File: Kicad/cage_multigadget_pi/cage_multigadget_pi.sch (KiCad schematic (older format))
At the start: 41 parts, among them J1 USB_B_Micro, J2 Raspberry_Pi_2_3, Q1 BSN20, Q2 BSN20, Q3 BSN20, Q4 BSN20, Q5 BSN20, U1 OP495, U2 MCP3004, U3 LED_shift_register_SPI, U4 MultigadgetDevice, U5 MultigadgetDevice, U6 LED_Button_connector, U7 LED_Button_connector, U8 LED_Button_connector, U9 LED_Button_connector

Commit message: added reward line, changed 2x40 pin header to 2x20 header, changed USB footprint and shifted
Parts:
- added J3: Conn_01x02, Socket_Strips:Socket_Strip_Straight_1x02_Pitch2.54mm, symbol Connector_Generic:Conn_01x02
- J1: footprint Connector_USB:USB_Micro-B_Amphenol_10103594-0001LF_Horizontal -> Digikey_footprints:USB_Micro_B_Female_10118194-0001LF
- J2: footprint Connector_PinSocket_2.54mm:PinSocket_2x40_P2.54mm_Vertical -> Pin_Headers:Pin_Header_Straight_2x20_Pitch2.54mm
- U3: symbol additional_LED_drivers:LED_shift_register_SPI -> cage_multigadget_pi-rescue:LED_shift_register_SPI-additional_LED_drivers
- U4, U5: symbol MillerLab_CommonComponents:MultigadgetDevice -> cage_multigadget_pi-rescue:MultigadgetDevice-MillerLab_CommonComponents
- U6, U7, U8, U9: symbol MillerLab_CommonComponents:LED_Button_connector -> cage_multigadget_pi-rescue:LED_Button_connector-MillerLab_CommonComponents
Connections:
- net labels added: Reward
- no-connect marks 42 -> 41
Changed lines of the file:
@@
 EESchema Schematic File Version 4
-LIBS:cage_multigadget_pi-cache
 EELAYER 30 0
 EELAYER END
@@
 F 0 "J1" H 1407 7017 50  0000 C CNN
 F 1 "USB_B_Micro" H 1407 6926 50  0000 C CNN
-F 2 "Connector_USB:USB_Micro-B_Amphenol_10103594-0001LF_Horizontal" H 1500 6500 50  0001 C CNN
+F 2 "Digikey_footprints:USB_Micro_B_Female_10118194-0001LF" H 1500 6500 50  0001 C CNN
 F 3 "~" H 1500 6500 50  0001 C CNN
 	1    1350 6550
@@
 NoConn ~ 10550 1450
 NoConn ~ 10550 1650
-NoConn ~ 10550 1750
 NoConn ~ 10550 1850
 NoConn ~ 10550 2050
@@
 F 0 "J2" H 9150 3650 50  0000 C CNN
 F 1 "Raspberry_Pi_2_3" H 9100 3550 50  0000 C CNN
-F 2 "Connector_PinSocket_2.54mm:PinSocket_2x40_P2.54mm_Vertical" H 9750 2250 50  0001 C CNN
+F 2 "Pin_Headers:Pin_Header_Straight_2x20_Pitch2.54mm" H 9750 2250 50  0001 C CNN
 F 3 "https://www.raspberrypi.org/documentation/hardware/raspberrypi/schematics/rpi_SCH_3bplus_1p0_reduced.pdf" H 9750 2250 50  0001 C CNN
 	1    9750 2250
@@
 Chip_Select_LED_3V
 $Comp
-L MillerLab_CommonComponents:MultigadgetDevice U4
+L cage_multigadget_pi-rescue:MultigadgetDevice-MillerLab_CommonComponents U4
 U 1 1 5E2EF314
 P 8200 3700
@@
 $EndComp
 $Comp
-L MillerLab_CommonComponents:MultigadgetDevice U5
+L cage_multigadget_pi-rescue:MultigadgetDevice-MillerLab_CommonComponents U5
 U 1 1 5E2F637C
 P 8200 4550
@@
 $EndComp
 $Comp
-L MillerLab_CommonComponents:LED_Button_connector U6
+L cage_multigadget_pi-rescue:LED_Button_connector-MillerLab_CommonComponents U6
 U 1 1 5E2FDD90
 P 10150 5550
@@
 $EndComp
 $Comp
-L MillerLab_CommonComponents:LED_Button_connector U7
+L cage_multigadget_pi-rescue:LED_Button_connector-MillerLab_CommonComponents U7
 U 1 1 5E2FEBB6
 P 10150 6050
@@
 	9600 6200 9750 6200
 $Comp
-L additional_LED_drivers:LED_shift_register_SPI U3
+L cage_multigadget_pi-rescue:LED_shift_register_SPI-additional_LED_drivers U3
 U 1 1 5E3E6FAF
 P 7000 1000
@@
 Device1LED
 $Comp
-L MillerLab_CommonComponents:LED_Button_connector U8
+L cage_multigadget_pi-rescue:LED_Button_connector-MillerLab_CommonComponents U8
 U 1 1 5E7FE5B8
 P 8150 5550
@@
 $EndComp
 $Comp
-L MillerLab_CommonComponents:LED_Button_connector U9
+L cage_multigadget_pi-rescue:LED_Button_connector-MillerLab_CommonComponents U9
 U 1 1 5E7FE5BE
 P 8150 6050
@@
 Wire Wire Line
 	5650 2050 6500 2050
+Text Label 10550 1750 0    50   ~ 0
+Reward
+$Comp
+L Connector_Generic:Conn_01x02 J3
+U 1 1 5E97ECE6
+P 10500 4050
+F 0 "J3" H 10580 4042 50  0000 L CNN
+F 1 "Conn_01x02" H 10580 3951 50  0000 L CNN
+F 2 "Socket_Strips:Socket_Strip_Straight_1x02_Pitch2.54mm" H 10500 4050 50  0001 C CNN
+F 3 "~" H 10500 4050 50  0001 C CNN
+	1    10500 4050
+	1    0    0    -1
+$EndComp
+Text Label 10300 4050 2    50   ~ 0
+Reward
+Text Label 10300 4150 2    50   ~ 0
+GND
 $EndSCHEMATC

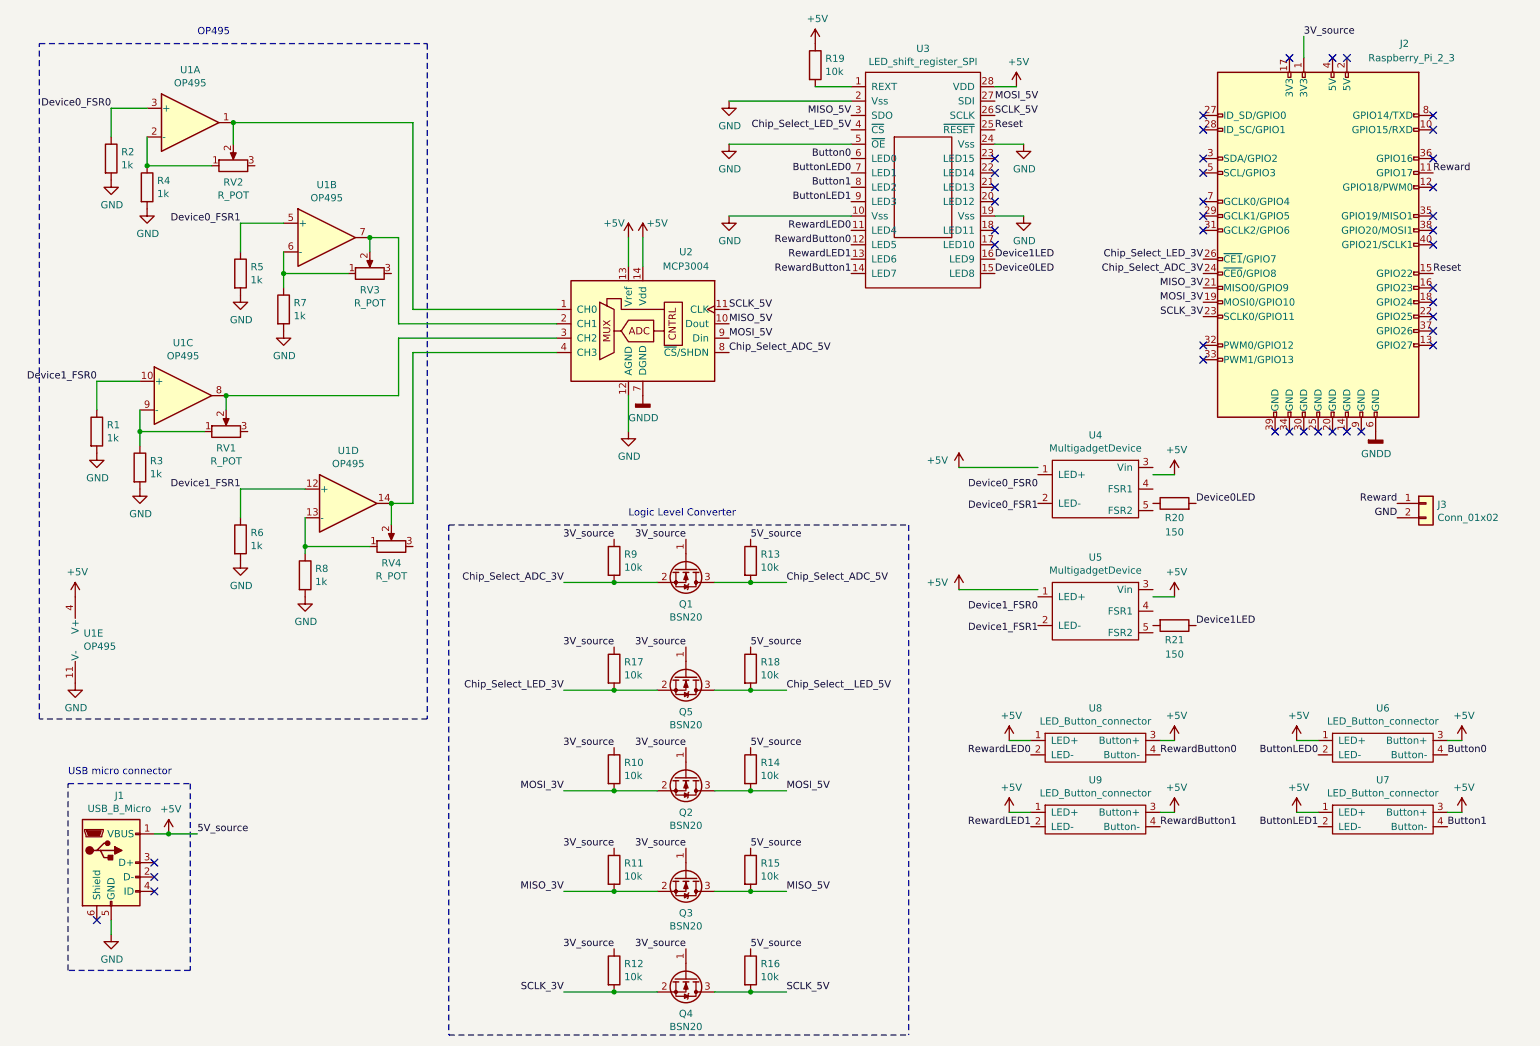
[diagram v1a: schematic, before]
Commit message: changes to the multigadget circuit
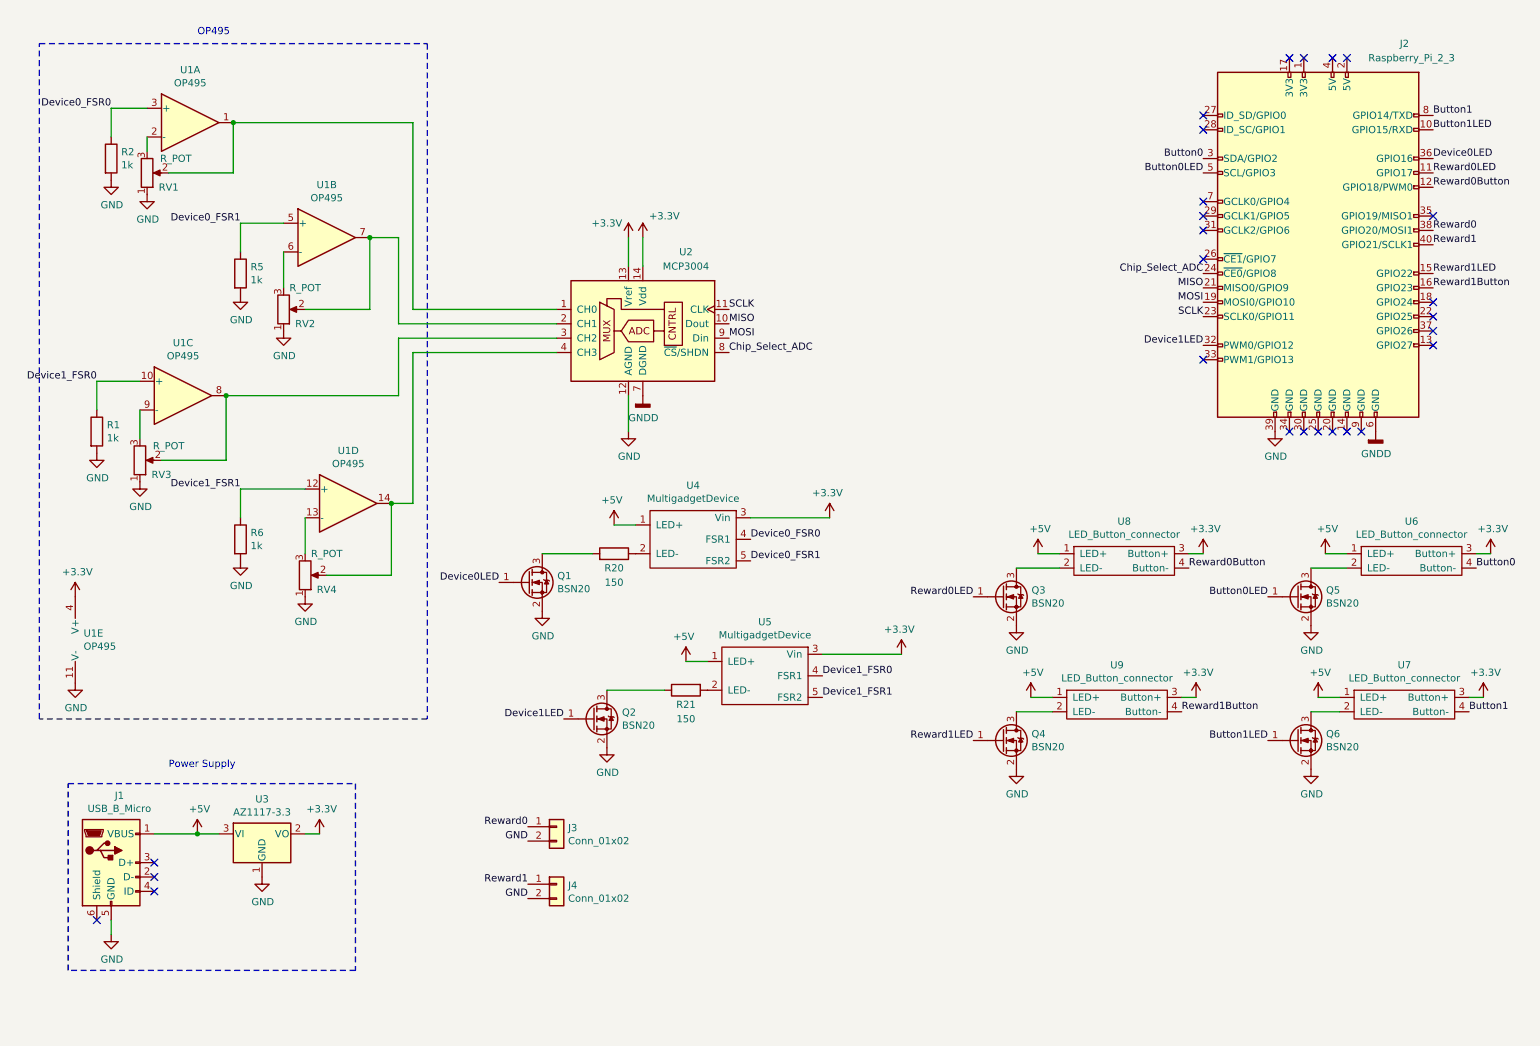
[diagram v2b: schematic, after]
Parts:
- removed R10, R11, R12, R13, R14, R15, R16, R17, R18, R19, R9: 10k, Resistor_SMD:R_1206_3216Metric_Pad1.42x1.75mm_HandSolder, symbol Device:R
- removed R3, R4, R7, R8: 1k, Resistor_SMD:R_1206_3216Metric_Pad1.42x1.75mm_HandSolder, symbol Device:R
- removed U3: LED_shift_register_SPI, Package_SO:HTSSOP-28-1EP_4.4x9.7mm_P0.65mm_EP3.4x9.5mm_Mask2.4x6.17mm, symbol cage_multigadget_pi-rescue:LED_shift_register_SPI-additional_LED_drivers
- added J4: Conn_01x02, Socket_Strips:Socket_Strip_Straight_1x02_Pitch2.54mm, symbol Connector_Generic:Conn_01x02
- added Q6: BSN20, TO_SOT_Packages_SMD:SOT-23, symbol Transistor_FET:BSN20
- added U3: AZ1117-3.3, TO_SOT_Packages_SMD:SOT-223, symbol Regulator_Linear:AZ1117-3.3
- Q1, Q2, Q3, Q4, Q5: footprint Package_TO_SOT_SMD:SOT-23 -> TO_SOT_Packages_SMD:SOT-23
- RV1, RV2, RV3, RV4: footprint Potentiometer_THT:Potentiometer_Bourns_3296Y_Vertical -> Potentiometers:Potentiometer_Trimmer_Bourns_3296Y
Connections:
- net labels added: +3.3V, Button0LED, Button1LED, Chip_Select_ADC, MISO, MOSI, Reward0, Reward0Button, Reward0LED, Reward1, Reward1Button, Reward1LED, SCLK
- net labels removed: 3V_source, 5V_source, ButtonLED0, ButtonLED1, Chip_Select_ADC_3V, Chip_Select_ADC_5V, Chip_Select_LED_3V, Chip_Select_LED_5V, Chip_Select__LED_5V, MISO_3V, MISO_5V, MOSI_3V, MOSI_5V, Reset, Reward, RewardButton0, RewardButton1, RewardLED0, RewardLED1, SCLK_3V, SCLK_5V
- wire segments 81 -> 57
- no-connect marks 41 -> 26
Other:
- note added: "Power Supply"
- note removed: "Logic Level Converter"
- note removed: "USB micro connector"
- moved on the sheet: J3, R20, R21, RV1, RV2, RV3, RV4, U4, U5, U6, U7, U8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

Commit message: updating the amplifier gain setup to so that it's actually going to work...
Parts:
- U4, U5: symbol cage_multigadget_pi-rescue:MultigadgetDevice-MillerLab_CommonComponents -> cage_multigadget_pi-rescue:MultigadgetDevice-MillerLab_CommonComponents-cage_multigadget_pi-rescue
- U6, U7, U8, U9: symbol cage_multigadget_pi-rescue:LED_Button_connector-MillerLab_CommonComponents -> cage_multigadget_pi-rescue:LED_Button_connector-MillerLab_CommonComponents-cage_multigadget_pi-rescue
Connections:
- net at U1.1, U2.1 (CH0): now also RV1.3; no longer RV1.2
- net at U1.2 (-): now also RV1.2; no longer RV1.3
- net at U1.6 (-): now also RV2.2; no longer RV2.3
- net at U1.7, U2.2 (CH1): now also RV2.3; no longer RV2.2
- net at U1.8, U2.3 (CH2): now also RV3.3; no longer RV3.2
- net at U1.9 (-): now also RV3.2; no longer RV3.3
- net at U1.13 (-): now also RV4.2; no longer RV4.3
- net at U1.14, U2.4 (CH3): now also RV4.3; no longer RV4.2
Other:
- moved on the sheet: RV1, RV2, RV3, RV4
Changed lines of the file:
@@
 L power:GND #PWR0103
 U 1 1 5DD82205
-P 2700 4700
-F 0 "#PWR0103" H 2700 4450 50  0001 C CNN
-F 1 "GND" H 2705 4527 50  0000 C CNN
-F 2 "" H 2700 4700 50  0001 C CNN
-F 3 "" H 2700 4700 50  0001 C CNN
-	1    2700 4700
+P 3350 4700
+F 0 "#PWR0103" H 3350 4450 50  0001 C CNN
+F 1 "GND" H 3355 4527 50  0000 C CNN
+F 2 "" H 3350 4700 50  0001 C CNN
+F 3 "" H 3350 4700 50  0001 C CNN
+	1    3350 4700
 	1    0    0    -1
 $EndComp
@@
 L power:GND #PWR0105
 U 1 1 5DD844C0
-P 1550 3900
-F 0 "#PWR0105" H 1550 3650 50  0001 C CNN
-F 1 "GND" H 1555 3727 50  0000 C CNN
-F 2 "" H 1550 3900 50  0001 C CNN
-F 3 "" H 1550 3900 50  0001 C CNN
-	1    1550 3900
-	1    0    0    -1
+P 2300 3700
+F 0 "#PWR0105" H 2300 3450 50  0001 C CNN
+F 1 "GND" H 2150 3600 50  0000 C CNN
+F 2 "" H 2300 3700 50  0001 C CNN
+F 3 "" H 2300 3700 50  0001 C CNN
+	1    2300 3700
+	-1   0    0    -1
 $EndComp
 $Comp
@@
 L power:GND #PWR0108
 U 1 1 5DD85905
-P 2550 2850
-F 0 "#PWR0108" H 2550 2600 50  0001 C CNN
-F 1 "GND" H 2555 2677 50  0000 C CNN
-F 2 "" H 2550 2850 50  0001 C CNN
-F 3 "" H 2550 2850 50  0001 C CNN
-	1    2550 2850
+P 3200 2700
+F 0 "#PWR0108" H 3200 2450 50  0001 C CNN
+F 1 "GND" H 3205 2527 50  0000 C CNN
+F 2 "" H 3200 2700 50  0001 C CNN
+F 3 "" H 3200 2700 50  0001 C CNN
+	1    3200 2700
 	1    0    0    -1
 $EndComp
@@
 L power:GND #PWR0109
 U 1 1 5DD86DF7
-P 1600 1900
-F 0 "#PWR0109" H 1600 1650 50  0001 C CNN
-F 1 "GND" H 1605 1727 50  0000 C CNN
-F 2 "" H 1600 1900 50  0001 C CNN
-F 3 "" H 1600 1900 50  0001 C CNN
-	1    1600 1900
+P 2350 1800
+F 0 "#PWR0109" H 2350 1550 50  0001 C CNN
+F 1 "GND" H 2355 1627 50  0000 C CNN
+F 2 "" H 2350 1800 50  0001 C CNN
+F 3 "" H 2350 1800 50  0001 C CNN
+	1    2350 1800
 	1    0    0    -1
 $EndComp
@@
 L Device:R_POT RV2
 U 1 1 5DDB9ACD
-P 2550 2700
-F 0 "RV2" H 2700 2800 50  0000 C CNN
-F 1 "R_POT" H 2700 2550 50  0000 C CNN
-F 2 "Potentiometers:Potentiometer_Trimmer_Bourns_3296Y" H 2550 2700 50  0001 C CNN
-F 3 "~" H 2550 2700 50  0001 C CNN
-	1    2550 2700
-	1    0    0    1
+P 3200 2550
+F 0 "RV2" H 3350 2650 50  0000 C CNN
+F 1 "R_POT" H 3350 2400 50  0000 C CNN
+F 2 "Potentiometers:Potentiometer_Trimmer_Bourns_3296Y" H 3200 2550 50  0001 C CNN
+F 3 "~" H 3200 2550 50  0001 C CNN
+	1    3200 2550
+	-1   0    0    1
 $EndComp
 $Comp
 L Device:R_POT RV3
 U 1 1 5DDC493C
-P 1550 3750
-F 0 "RV3" H 1700 3850 50  0000 C CNN
-F 1 "R_POT" H 1750 3650 50  0000 C CNN
-F 2 "Potentiometers:Potentiometer_Trimmer_Bourns_3296Y" H 1550 3750 50  0001 C CNN
-F 3 "~" H 1550 3750 50  0001 C CNN
-	1    1550 3750
-	1    0    0    1
+P 2300 3550
+F 0 "RV3" H 2450 3650 50  0000 C CNN
+F 1 "R_POT" H 2500 3450 50  0000 C CNN
+F 2 "Potentiometers:Potentiometer_Trimmer_Bourns_3296Y" H 2300 3550 50  0001 C CNN
+F 3 "~" H 2300 3550 50  0001 C CNN
+	1    2300 3550
+	-1   0    0    1
 $EndComp
 $Comp
 L Device:R_POT RV4
 U 1 1 5DDC696E
-P 2700 4550
-F 0 "RV4" H 2850 4650 50  0000 C CNN
-F 1 "R_POT" H 2850 4400 50  0000 C CNN
-F 2 "Potentiometers:Potentiometer_Trimmer_Bourns_3296Y" H 2700 4550 50  0001 C CNN
-F 3 "~" H 2700 4550 50  0001 C CNN
-	1    2700 4550
-	1    0    0    1
-$EndComp
-Wire Wire Line
-	1600 1500 1600 1600
+P 3350 4550
+F 0 "RV4" H 3500 4650 50  0000 C CNN
+F 1 "R_POT" H 3500 4400 50  0000 C CNN
+F 2 "Potentiometers:Potentiometer_Trimmer_Bourns_3296Y" H 3350 4550 50  0001 C CNN
+F 3 "~" H 3350 4550 50  0001 C CNN
+	1    3350 4550
+	-1   0    0    1
+$EndComp
 Wire Wire Line
 	1350 1500 1350 1300
@@
 $EndComp
 Wire Wire Line
-	3300 4050 3450 4050
+	3300 4050 3350 4050
 Wire Wire Line
 	3450 4050 3450 3000
-Connection ~ 3300 4050
 $Comp
 L Connector:USB_B_Micro J1
@@
 OP495
 $Comp
-L cage_multigadget_pi-rescue:MultigadgetDevice-MillerLab_CommonComponents U4
+L cage_multigadget_pi-rescue:MultigadgetDevice-MillerLab_CommonComponents-cage_multigadget_pi-rescue U4
 U 1 1 5E2EF314
 P 5400 4050
@@
 $EndComp
 $Comp
-L cage_multigadget_pi-rescue:MultigadgetDevice-MillerLab_CommonComponents U5
+L cage_multigadget_pi-rescue:MultigadgetDevice-MillerLab_CommonComponents-cage_multigadget_pi-rescue U5
 U 1 1 5E2F637C
 P 5900 5000
@@
 $EndComp
 $Comp
-L cage_multigadget_pi-rescue:LED_Button_connector-MillerLab_CommonComponents U6
+L cage_multigadget_pi-rescue:LED_Button_connector-MillerLab_CommonComponents-cage_multigadget_pi-rescue U6
 U 1 1 5E2FDD90
 P 10350 4250
@@
 $EndComp
 $Comp
-L cage_multigadget_pi-rescue:LED_Button_connector-MillerLab_CommonComponents U7
+L cage_multigadget_pi-rescue:LED_Button_connector-MillerLab_CommonComponents-cage_multigadget_pi-rescue U7
 U 1 1 5E2FEBB6
 P 10300 5250
@@
 	3350 2900 3350 3300
 Wire Wire Line
-	3350 3300 2150 3300
+	3350 3300 2300 3300
 Wire Wire Line
 	3350 2900 4450 2900
-Connection ~ 2150 3300
-Wire Wire Line
-	3150 2200 3350 2200
+Wire Wire Line
+	3150 2200 3200 2200
 Wire Wire Line
 	3350 2200 3350 2800
 Wire Wire Line
 	3350 2800 4450 2800
-Connection ~ 3150 2200
 Wire Wire Line
 	3450 2700 3450 1400
 Wire Wire Line
-	3450 1400 2200 1400
+	3450 1400 2350 1400
 Wire Wire Line
 	3450 2700 4450 2700
-Connection ~ 2200 1400
-$Comp
-L cage_multigadget_pi-rescue:LED_Button_connector-MillerLab_CommonComponents U8
+$Comp
+L cage_multigadget_pi-rescue:LED_Button_connector-MillerLab_CommonComponents-cage_multigadget_pi-rescue U8
 U 1 1 5E7FE5B8
 P 8350 4250
@@
 $EndComp
 $Comp
-L cage_multigadget_pi-rescue:LED_Button_connector-MillerLab_CommonComponents U9
+L cage_multigadget_pi-rescue:LED_Button_connector-MillerLab_CommonComponents-cage_multigadget_pi-rescue U9
 U 1 1 5E7FE5BE
 P 8300 5250
@@
 Button1LED
 Wire Wire Line
-	2200 1400 2200 1750
-Wire Wire Line
-	1750 1750 2200 1750
-Wire Wire Line
-	2550 2300 2550 2550
-Wire Wire Line
-	2700 2700 3150 2700
-Wire Wire Line
-	3150 2200 3150 2700
-Wire Wire Line
-	1550 3400 1550 3600
-Wire Wire Line
-	1700 3750 2150 3750
-Wire Wire Line
-	2150 3300 2150 3750
-Wire Wire Line
-	2700 4150 2700 4400
-Wire Wire Line
-	2850 4550 3300 4550
-Wire Wire Line
-	3300 4050 3300 4550
+	1550 3400 1550 3550
 $Comp
 L power:GND #PWR0138
@@
 L Device:R_POT RV1
 U 1 1 5DDC4EC4
-P 1600 1750
-F 0 "RV1" H 1750 1850 50  0000 C CNN
-F 1 "R_POT" H 1800 1650 50  0000 C CNN
-F 2 "Potentiometers:Potentiometer_Trimmer_Bourns_3296Y" H 1600 1750 50  0001 C CNN
-F 3 "~" H 1600 1750 50  0001 C CNN
-	1    1600 1750
-	1    0    0    1
-$EndComp
+P 2350 1650
+F 0 "RV1" H 2500 1750 50  0000 C CNN
+F 1 "R_POT" H 2550 1550 50  0000 C CNN
+F 2 "Potentiometers:Potentiometer_Trimmer_Bourns_3296Y" H 2350 1650 50  0001 C CNN
+F 3 "~" H 2350 1650 50  0001 C CNN
+	1    2350 1650
+	-1   0    0    1
+$EndComp
+Wire Wire Line
+	3350 4400 3350 4050
+Connection ~ 3350 4050
+Wire Wire Line
+	3350 4050 3450 4050
+Wire Wire Line
+	2700 4550 3200 4550
+Wire Wire Line
+	2700 4150 2700 4550
+Wire Wire Line
+	2150 3550 1550 3550
+Wire Wire Line
+	2300 3400 2300 3300
+Connection ~ 2300 3300
+Wire Wire Line
+	2300 3300 2150 3300
+Wire Wire Line
+	3200 2400 3200 2200
+Connection ~ 3200 2200
+Wire Wire Line
+	3200 2200 3350 2200
+Wire Wire Line
+	2550 2300 2550 2550
+Wire Wire Line
+	2550 2550 3050 2550
+Wire Wire Line
+	2350 1500 2350 1400
+Connection ~ 2350 1400
+Wire Wire Line
+	2350 1400 2200 1400
+Wire Wire Line
+	2200 1650 1600 1650
+Wire Wire Line
+	1600 1650 1600 1500
 $EndSCHEMATC
